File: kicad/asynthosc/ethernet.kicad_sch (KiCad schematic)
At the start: 39 parts, among them J3 RJ45_LED_Shielded, U5 LAN8742A, U6 USBLC6-2P6, Y2 25MHZ,20PF,30PPM

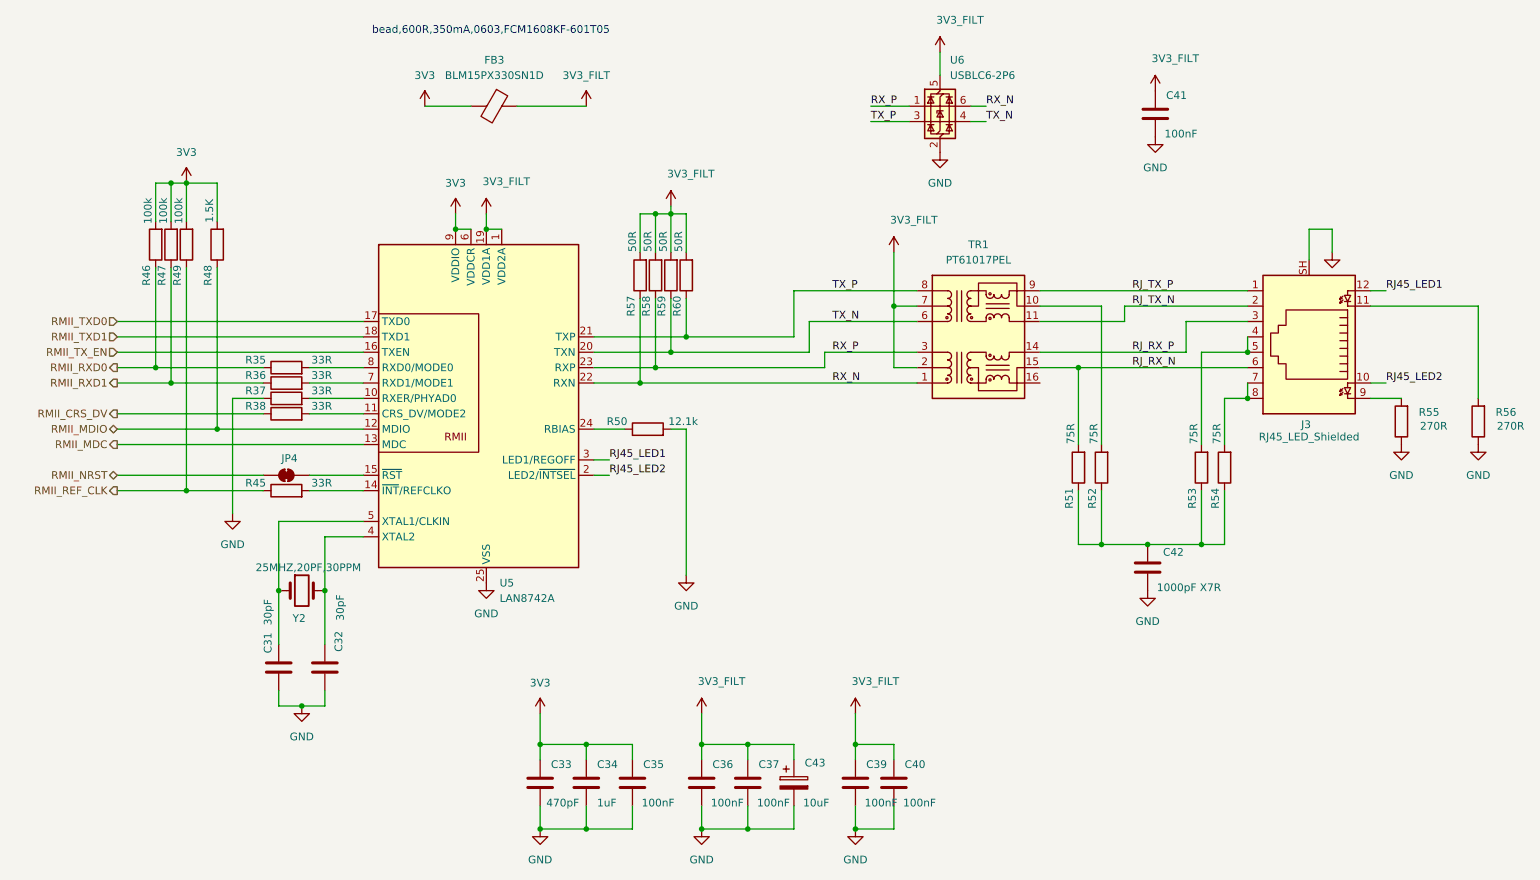
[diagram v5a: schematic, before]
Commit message: bom: update bom for lcsc
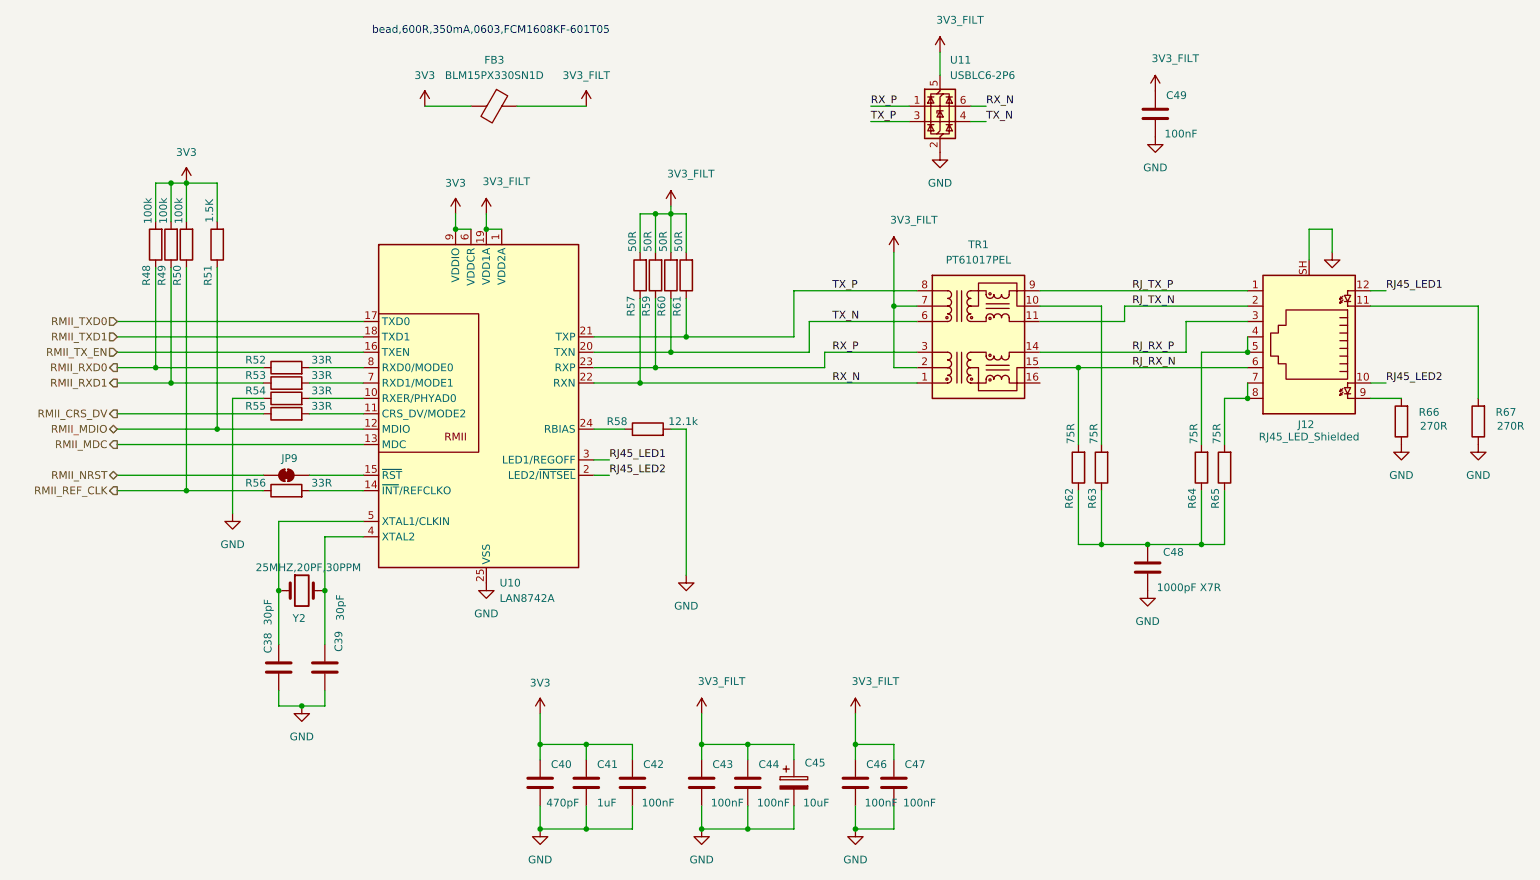
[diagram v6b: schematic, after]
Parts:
- C45: renamed from C43; Manufacturer (none) -> Roqang; RefNum (none) -> RVT1V100M0405
- JP9: renamed from JP4; RefNum (none) -> _na_
- R48: renamed from R46; RefNum (none) -> _generic_
- R49: renamed from R47; RefNum (none) -> _generic_
- R50: renamed from R49; RefNum (none) -> _generic_
- R51: renamed from R48; RefNum (none) -> _generic_
- R52: renamed from R35; RefNum (none) -> _generic_
- R53: renamed from R36; RefNum (none) -> _generic_
- R54: renamed from R37; RefNum (none) -> _generic_
- R55: renamed from R38; RefNum (none) -> _generic_
- R56: renamed from R45; RefNum (none) -> _generic_
- R57: RefNum (none) -> _generic_
- R58: renamed from R50; RefNum (none) -> _generic_
- R59: renamed from R58; RefNum (none) -> _generic_
- R60: renamed from R59; RefNum (none) -> _generic_
- R61: renamed from R60; RefNum (none) -> _generic_
- R62: renamed from R51; RefNum (none) -> _generic_
- R63: renamed from R52; RefNum (none) -> _generic_
- R64: renamed from R53; RefNum (none) -> _generic_
- R65: renamed from R54; RefNum (none) -> _generic_
- R66: renamed from R55; RefNum (none) -> _generic_
- R67: renamed from R56; RefNum (none) -> _generic_
- U11: renamed from U6; Manufacturer ST -> STMicroelectronics
- Y2: Manufacturer (none) -> YXC; RefNum X53T-C20SSA-25.000MHz -> X322525MOB4SI
- renumbered C31 to C38, C32 to C39, C33 to C40, C34 to C41, C35 to C42, C36 to C43, C37 to C44, C39 to C46, C40 to C47, C42 to C48, C41 to C49, J3 to J12, U5 to U10

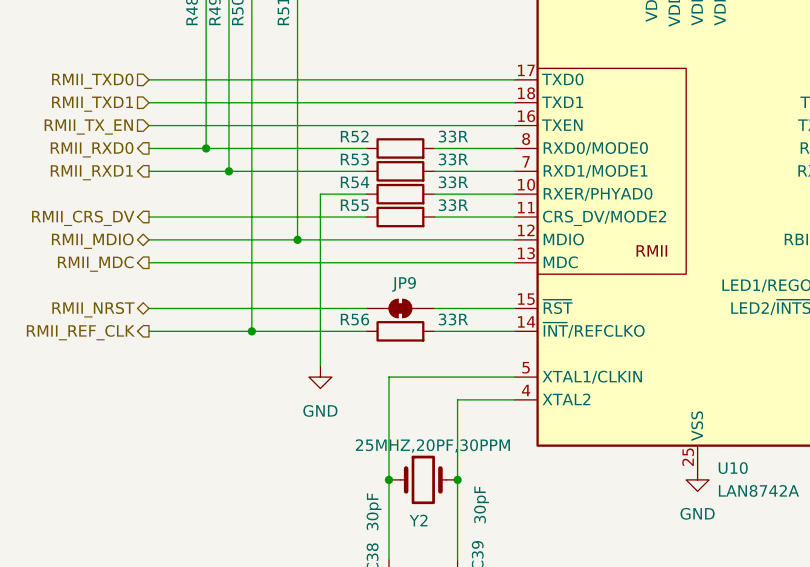
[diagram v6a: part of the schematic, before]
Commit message: pcb: place and change some components for easier routing
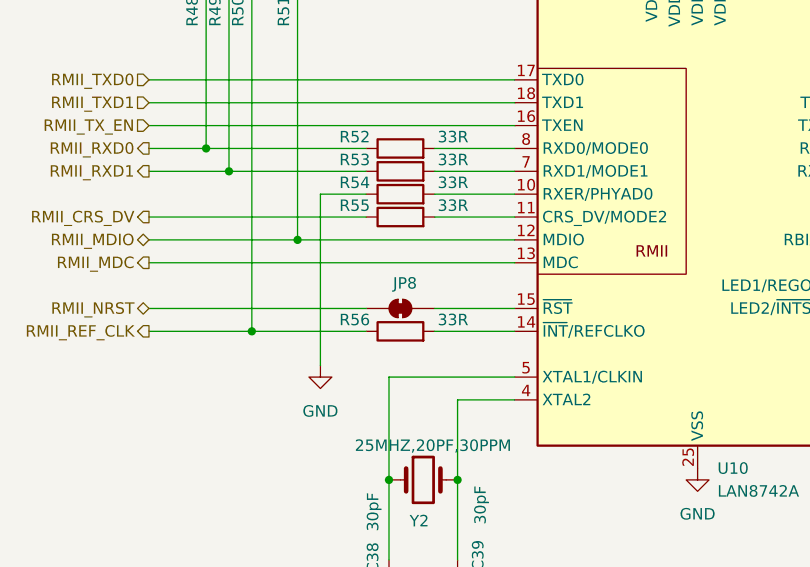
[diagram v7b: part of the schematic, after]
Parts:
- renumbered JP9 to JP8
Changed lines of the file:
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@@
 		(on_board yes)
 		(dnp no)
-		(property "Reference" "#PWR0103"
+		(property "Reference" "#PWR0106"
 			(at 125.73 135.89 0)
 			(effects
@@
 			(project "asynthosc"
 				(path "/d73e377a-a016-415f-8824-91cc6e4907b9/dee5e89d-6774-4f8d-b6d8-6a859b9e32e8/354f1097-74a0-4bc1-8721-d2c0e4c9dab3"
-					(reference "#PWR0103")
+					(reference "#PWR0106")
 					(unit 1)
 				)
@@
 		(dnp no)
 		(fields_autoplaced yes)
-		(property "Reference" "#PWR0115"
+		(property "Reference" "#PWR0118"
 			(at 254 93.98 0)
 			(effects
@@
 			(project "asynthosc"
 				(path "/d73e377a-a016-415f-8824-91cc6e4907b9/dee5e89d-6774-4f8d-b6d8-6a859b9e32e8/354f1097-74a0-4bc1-8721-d2c0e4c9dab3"
-					(reference "#PWR0115")
+					(reference "#PWR0118")
 					(unit 1)
 				)
@@
 		(dnp no)
 		(fields_autoplaced yes)
-		(property "Reference" "#PWR0112"
+		(property "Reference" "#PWR0115"
 			(at 200.66 43.18 0)
 			(effects
@@
 			(project "asynthosc"
 				(path "/d73e377a-a016-415f-8824-91cc6e4907b9/dee5e89d-6774-4f8d-b6d8-6a859b9e32e8/354f1097-74a0-4bc1-8721-d2c0e4c9dab3"
-					(reference "#PWR0112")
+					(reference "#PWR0115")
 					(unit 1)
 				)
@@
 		(dnp no)
 		(fields_autoplaced yes)
-		(property "Reference" "#PWR098"
+		(property "Reference" "#PWR0101"
 			(at 99.06 135.89 0)
 			(effects
@@
 			(project "asynthosc"
 				(path "/d73e377a-a016-415f-8824-91cc6e4907b9/dee5e89d-6774-4f8d-b6d8-6a859b9e32e8/354f1097-74a0-4bc1-8721-d2c0e4c9dab3"
-					(reference "#PWR098")
+					(reference "#PWR0101")
 					(unit 1)
 				)
@@
 		(on_board yes)
 		(dnp no)
-		(property "Reference" "#PWR0107"
+		(property "Reference" "#PWR0110"
 			(at 157.48 59.69 0)
 			(effects
@@
 			(project "asynthosc"
 				(path "/d73e377a-a016-415f-8824-91cc6e4907b9/dee5e89d-6774-4f8d-b6d8-6a859b9e32e8/354f1097-74a0-4bc1-8721-d2c0e4c9dab3"
-					(reference "#PWR0107")
+					(reference "#PWR0110")
 					(unit 1)
 				)
@@
 		(on_board yes)
 		(dnp no)
-		(property "Reference" "#PWR0101"
+		(property "Reference" "#PWR0104"
 			(at 120.65 52.07 0)
 			(effects
@@
 			(project "asynthosc"
 				(path "/d73e377a-a016-415f-8824-91cc6e4907b9/dee5e89d-6774-4f8d-b6d8-6a859b9e32e8/354f1097-74a0-4bc1-8721-d2c0e4c9dab3"
-					(reference "#PWR0101")
+					(reference "#PWR0104")
 					(unit 1)
 				)
@@
 		(dnp no)
 		(fields_autoplaced yes)
-		(property "Reference" "#PWR0102"
+		(property "Reference" "#PWR0105"
 			(at 123.19 115.57 0)
 			(effects
@@
 			(project "asynthosc"
 				(path "/d73e377a-a016-415f-8824-91cc6e4907b9/dee5e89d-6774-4f8d-b6d8-6a859b9e32e8/354f1097-74a0-4bc1-8721-d2c0e4c9dab3"
-					(reference "#PWR0102")
+					(reference "#PWR0105")
 					(unit 1)
 				)
@@
 		(dnp no)
 		(fields_autoplaced yes)
-		(property "Reference" "#PWR093"
+		(property "Reference" "#PWR096"
 			(at 59.69 137.16 0)
 			(effects
@@
 			(project "asynthosc"
 				(path "/d73e377a-a016-415f-8824-91cc6e4907b9/dee5e89d-6774-4f8d-b6d8-6a859b9e32e8/354f1097-74a0-4bc1-8721-d2c0e4c9dab3"
-					(reference "#PWR093")
+					(reference "#PWR096")
 					(unit 1)
 				)
@@
 		(on_board yes)
 		(dnp no)
-		(property "Reference" "JP9"
+		(property "Reference" "JP8"
 			(at 57.658 89.916 0)
 			(effects
@@
 			(project "asynthosc"
 				(path "/d73e377a-a016-415f-8824-91cc6e4907b9/dee5e89d-6774-4f8d-b6d8-6a859b9e32e8/354f1097-74a0-4bc1-8721-d2c0e4c9dab3"
-					(reference "JP9")
+					(reference "JP8")
 					(unit 1)
 				)
@@
 		(dnp no)
 		(fields_autoplaced yes)
-		(property "Reference" "#PWR099"
+		(property "Reference" "#PWR0102"
 			(at 99.06 157.48 0)
 			(effects
@@
 			(project "asynthosc"
 				(path "/d73e377a-a016-415f-8824-91cc6e4907b9/dee5e89d-6774-4f8d-b6d8-6a859b9e32e8/354f1097-74a0-4bc1-8721-d2c0e4c9dab3"
-					(reference "#PWR099")
+					(reference "#PWR0102")
 					(unit 1)
 				)
@@
 		(on_board yes)
 		(dnp no)
-		(property "Reference" "#PWR096"
+		(property "Reference" "#PWR099"
 			(at 90.17 53.34 0)
 			(effects
@@
 			(project "asynthosc"
 				(path "/d73e377a-a016-415f-8824-91cc6e4907b9/dee5e89d-6774-4f8d-b6d8-6a859b9e32e8/354f1097-74a0-4bc1-8721-d2c0e4c9dab3"
-					(reference "#PWR096")
+					(reference "#PWR099")
 					(unit 1)
 				)
@@
 		(dnp no)
 		(fields_autoplaced yes)
-		(property "Reference" "#PWR0110"
+		(property "Reference" "#PWR0113"
 			(at 199.39 118.11 0)
 			(effects
@@
 			(project "asynthosc"
 				(path "/d73e377a-a016-415f-8824-91cc6e4907b9/dee5e89d-6774-4f8d-b6d8-6a859b9e32e8/354f1097-74a0-4bc1-8721-d2c0e4c9dab3"
-					(reference "#PWR0110")
+					(reference "#PWR0113")
 					(unit 1)
 				)
@@
 		(dnp no)
 		(fields_autoplaced yes)
-		(property "Reference" "#PWR095"
+		(property "Reference" "#PWR098"
 			(at 85.09 53.34 0)
 			(effects
@@
 			(project "asynthosc"
 				(path "/d73e377a-a016-415f-8824-91cc6e4907b9/dee5e89d-6774-4f8d-b6d8-6a859b9e32e8/354f1097-74a0-4bc1-8721-d2c0e4c9dab3"
-					(reference "#PWR095")
+					(reference "#PWR098")
 					(unit 1)
 				)
@@
 		(dnp no)
 		(fields_autoplaced yes)
-		(property "Reference" "#PWR091"
+		(property "Reference" "#PWR094"
 			(at 40.64 48.26 0)
 			(effects
@@
 			(project "asynthosc"
 				(path "/d73e377a-a016-415f-8824-91cc6e4907b9/dee5e89d-6774-4f8d-b6d8-6a859b9e32e8/354f1097-74a0-4bc1-8721-d2c0e4c9dab3"
-					(reference "#PWR091")
+					(reference "#PWR094")
 					(unit 1)
 				)
@@
 		(on_board yes)
 		(dnp no)
-		(property "Reference" "#PWR0108"
+		(property "Reference" "#PWR0111"
 			(at 165.1 26.67 0)
 			(effects
@@
 			(project "asynthosc"
 				(path "/d73e377a-a016-415f-8824-91cc6e4907b9/dee5e89d-6774-4f8d-b6d8-6a859b9e32e8/354f1097-74a0-4bc1-8721-d2c0e4c9dab3"
-					(reference "#PWR0108")
+					(reference "#PWR0111")
 					(unit 1)
 				)
@@
 		(on_board yes)
 		(dnp no)
-		(property "Reference" "#PWR0105"
+		(property "Reference" "#PWR0108"
 			(at 151.13 135.89 0)
 			(effects
@@
 			(project "asynthosc"
 				(path "/d73e377a-a016-415f-8824-91cc6e4907b9/dee5e89d-6774-4f8d-b6d8-6a859b9e32e8/354f1097-74a0-4bc1-8721-d2c0e4c9dab3"
-					(reference "#PWR0105")
+					(reference "#PWR0108")
 					(unit 1)
 				)
@@
 		(dnp no)
 		(fields_autoplaced yes)
-		(property "Reference" "#PWR0106"
+		(property "Reference" "#PWR0109"
 			(at 151.13 157.48 0)
 			(effects
@@
 			(project "asynthosc"
 				(path "/d73e377a-a016-415f-8824-91cc6e4907b9/dee5e89d-6774-4f8d-b6d8-6a859b9e32e8/354f1097-74a0-4bc1-8721-d2c0e4c9dab3"
-					(reference "#PWR0106")
+					(reference "#PWR0109")
 					(unit 1)
 				)
@@
 		(dnp no)
 		(fields_autoplaced yes)
-		(property "Reference" "#PWR094"
+		(property "Reference" "#PWR097"
 			(at 80.01 35.56 0)
 			(effects
@@
 			(project "asynthosc"
 				(path "/d73e377a-a016-415f-8824-91cc6e4907b9/dee5e89d-6774-4f8d-b6d8-6a859b9e32e8/354f1097-74a0-4bc1-8721-d2c0e4c9dab3"
-					(reference "#PWR094")
+					(reference "#PWR097")
 					(unit 1)
 				)
@@
 		(dnp no)
 		(fields_autoplaced yes)
-		(property "Reference" "#PWR0100"
+		(property "Reference" "#PWR0103"
 			(at 106.68 35.56 0)
 			(effects
@@
 			(project "asynthosc"
 				(path "/d73e377a-a016-415f-8824-91cc6e4907b9/dee5e89d-6774-4f8d-b6d8-6a859b9e32e8/354f1097-74a0-4bc1-8721-d2c0e4c9dab3"
-					(reference "#PWR0100")
+					(reference "#PWR0103")
 					(unit 1)
 				)
@@
 		(dnp no)
 		(fields_autoplaced yes)
-		(property "Reference" "#PWR097"
+		(property "Reference" "#PWR0100"
 			(at 90.17 116.84 0)
 			(effects
@@
 			(project "asynthosc"
 				(path "/d73e377a-a016-415f-8824-91cc6e4907b9/dee5e89d-6774-4f8d-b6d8-6a859b9e32e8/354f1097-74a0-4bc1-8721-d2c0e4c9dab3"
-					(reference "#PWR097")
+					(reference "#PWR0100")
 					(unit 1)
 				)
@@
 		(dnp no)
 		(fields_autoplaced yes)
-		(property "Reference" "#PWR0109"
+		(property "Reference" "#PWR0112"
 			(at 165.1 45.72 0)
 			(effects
@@
 			(project "asynthosc"
 				(path "/d73e377a-a016-415f-8824-91cc6e4907b9/dee5e89d-6774-4f8d-b6d8-6a859b9e32e8/354f1097-74a0-4bc1-8721-d2c0e4c9dab3"
-					(reference "#PWR0109")
+					(reference "#PWR0112")
 					(unit 1)
 				)
@@
 		(dnp no)
 		(fields_autoplaced yes)
-		(property "Reference" "#PWR092"
+		(property "Reference" "#PWR095"
 			(at 48.26 105.41 0)
 			(effects
@@
 			(project "asynthosc"
 				(path "/d73e377a-a016-415f-8824-91cc6e4907b9/dee5e89d-6774-4f8d-b6d8-6a859b9e32e8/354f1097-74a0-4bc1-8721-d2c0e4c9dab3"
-					(reference "#PWR092")
+					(reference "#PWR095")
 					(unit 1)
 				)
@@
 		(dnp no)
 		(fields_autoplaced yes)
-		(property "Reference" "#PWR0104"
+		(property "Reference" "#PWR0107"
 			(at 125.73 157.48 0)
 			(effects
@@
 			(project "asynthosc"
 				(path "/d73e377a-a016-415f-8824-91cc6e4907b9/dee5e89d-6774-4f8d-b6d8-6a859b9e32e8/354f1097-74a0-4bc1-8721-d2c0e4c9dab3"
-					(reference "#PWR0104")
+					(reference "#PWR0107")
 					(unit 1)
 				)
@@
 		(dnp no)
 		(fields_autoplaced yes)
-		(property "Reference" "#PWR0114"
+		(property "Reference" "#PWR0117"
 			(at 241.3 93.98 0)
 			(effects
@@
 			(project "asynthosc"
 				(path "/d73e377a-a016-415f-8824-91cc6e4907b9/dee5e89d-6774-4f8d-b6d8-6a859b9e32e8/354f1097-74a0-4bc1-8721-d2c0e4c9dab3"
-					(reference "#PWR0114")
+					(reference "#PWR0117")
 					(unit 1)
 				)
@@
 		(on_board yes)
 		(dnp no)
-		(property "Reference" "#PWR0111"
+		(property "Reference" "#PWR0114"
 			(at 200.66 33.02 0)
 			(effects
@@
 			(project "asynthosc"
 				(path "/d73e377a-a016-415f-8824-91cc6e4907b9/dee5e89d-6774-4f8d-b6d8-6a859b9e32e8/354f1097-74a0-4bc1-8721-d2c0e4c9dab3"
-					(reference "#PWR0111")
+					(reference "#PWR0114")
 					(unit 1)
 				)
@@
 		(dnp no)
 		(fields_autoplaced yes)
-		(property "Reference" "#PWR0113"
+		(property "Reference" "#PWR0116"
 			(at 229.87 62.23 0)
 			(effects
@@
 			(project "asynthosc"
 				(path "/d73e377a-a016-415f-8824-91cc6e4907b9/dee5e89d-6774-4f8d-b6d8-6a859b9e32e8/354f1097-74a0-4bc1-8721-d2c0e4c9dab3"
-					(reference "#PWR0113")
+					(reference "#PWR0116")
 					(unit 1)
 				)

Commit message: pcb: place and draft route
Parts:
- added U13: USBLC6-2P6, Package_TO_SOT_SMD:SOT-666, symbol Power_Protection:USBLC6-2P6
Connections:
- net 3V3_FILT: now also U13.5 (VBUS)
- net GND: now also U13.2 (GND)
- net RX_N: now also U11.3 (I/O2), U11.4 (I/O2); no longer U11.6 (I/O1)
- net RX_P: now also U11.6 (I/O1)
- net TX_N: now also U13.3 (I/O2), U13.4 (I/O2); no longer U11.4 (I/O2)
- net TX_P: now also U13.1 (I/O1), U13.6 (I/O1); no longer U11.3 (I/O2)
